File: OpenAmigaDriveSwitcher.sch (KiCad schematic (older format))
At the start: 7 parts, among them J1 PADS, J2 SWITCH, J99 OSHW_LOGO, U1 74LS157, U8 EVEN_CIA_CHIP

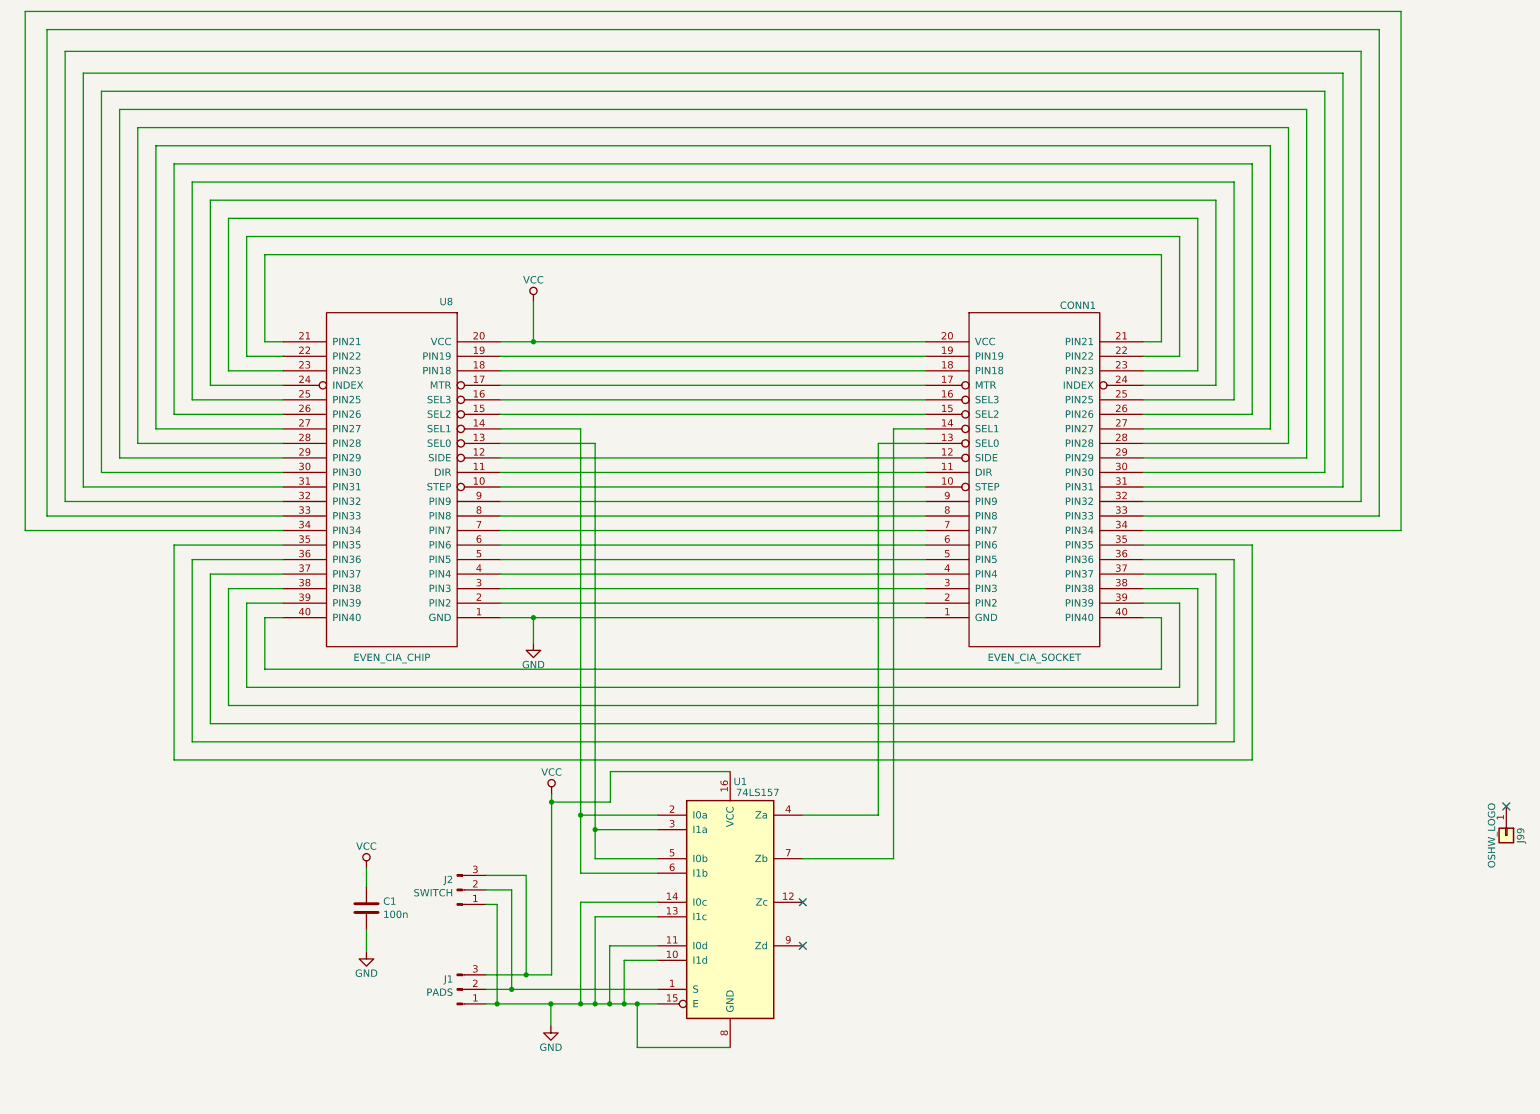
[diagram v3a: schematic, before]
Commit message: Allow swapping DF0 <-> DF2
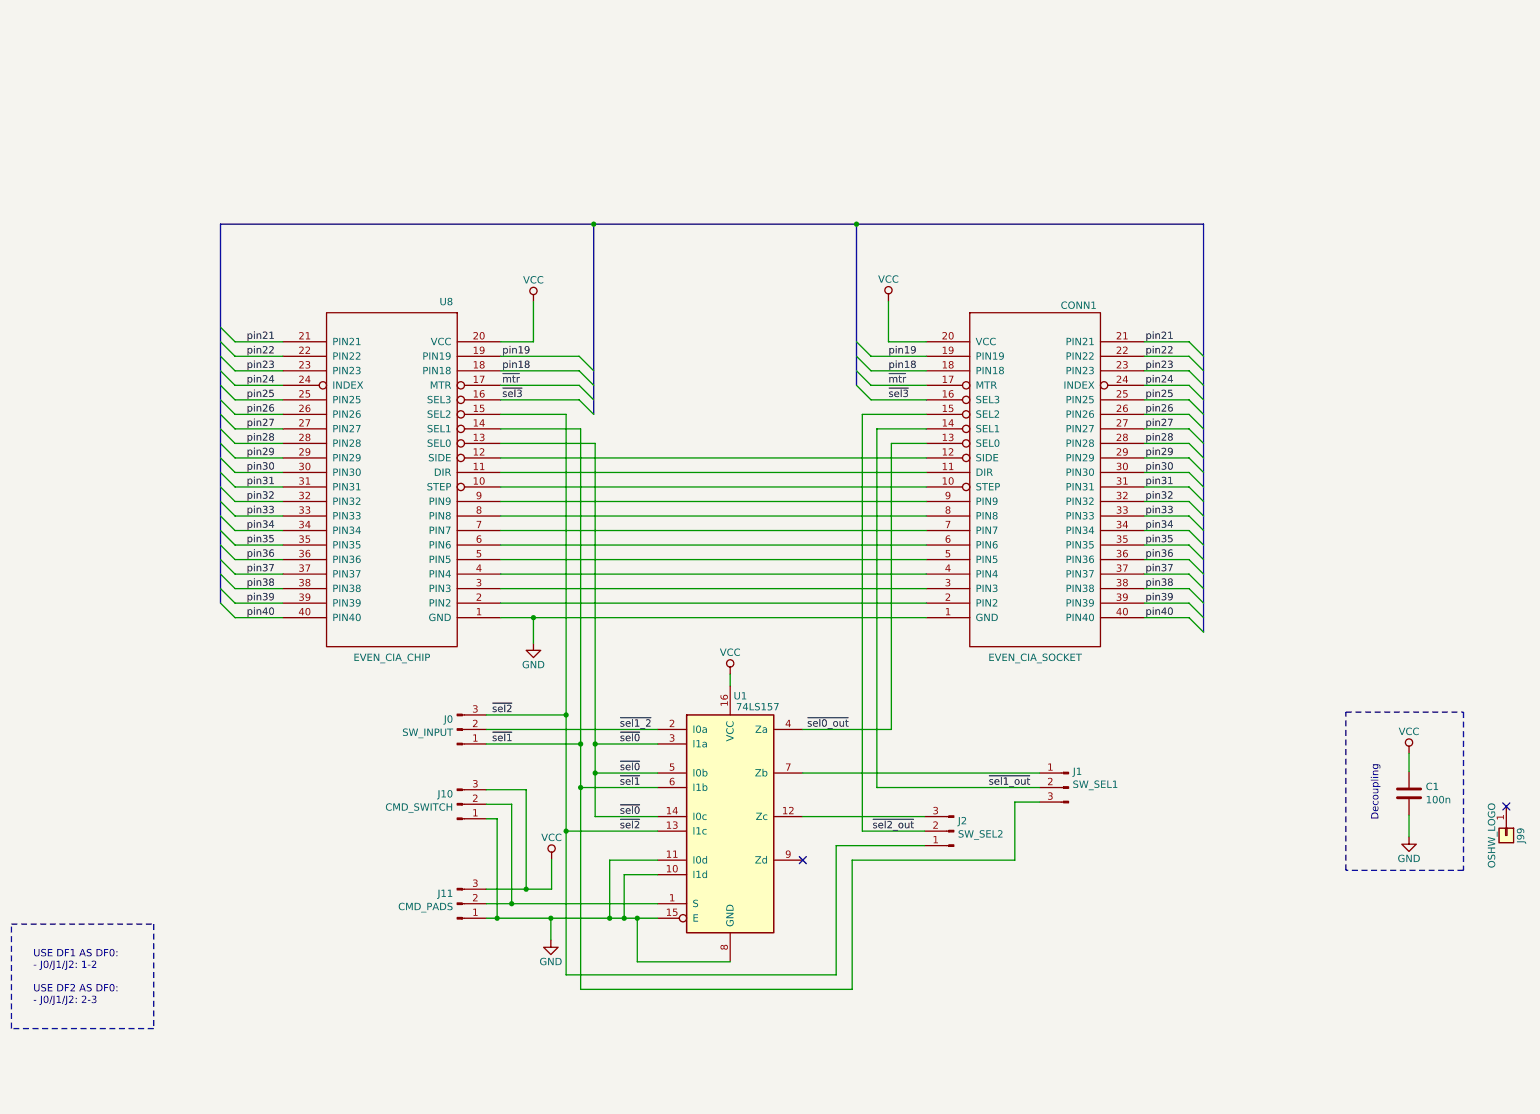
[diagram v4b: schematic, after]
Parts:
- added J0: SW_INPUT, OpenAmigaDriveSwitcher:SolderJumper-3_P1.3mm_Bridged12_RoundedPad1.0x1.5mm, symbol Connector:Conn_01x03_Male
- added J1: SW_SEL1, OpenAmigaDriveSwitcher:SolderJumper-3_P1.3mm_Bridged12_RoundedPad1.0x1.5mm, symbol Connector:Conn_01x03_Male
- added J2: SW_SEL2, OpenAmigaDriveSwitcher:SolderJumper-3_P1.3mm_Bridged12_RoundedPad1.0x1.5mm, symbol Connector:Conn_01x03_Male
- J10: renamed from J2; value SWITCH -> CMD_SWITCH
- J11: renamed from J1; value PADS -> CMD_PADS
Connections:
- net GND: no longer U1.13 (I1c), U1.14 (I0c)
- net ~sel0: now reaches U1.3 (I1a), U1.5 (I0b), U8.13 (SEL0)
- net ~sel0: now also U1.14 (I0c)
- net ~sel1: now reaches U1.6 (I1b), U8.14 (SEL1)
- net ~sel1: now also J0.1 (Pin_1), J1.3 (Pin_3); no longer U1.2 (I0a)
- net ~sel2: now reaches U8.15 (SEL2)
- net ~sel2: now also U1.13 (I1c), J0.3 (Pin_3), J2.1 (Pin_1); no longer CONN1.15 (SEL2)
- net ~sel3: now reaches CONN1.16 (SEL3), U8.16 (SEL3)
- net ~mtr: now reaches CONN1.17 (MTR), U8.17 (MTR)
- net pin18: now reaches CONN1.18 (PIN18), U8.18 (PIN18)
- net pin19: now reaches CONN1.19 (PIN19), U8.19 (PIN19)
- net pin21: now reaches CONN1.21 (PIN21), U8.21 (PIN21)
- net pin22: now reaches CONN1.22 (PIN22), U8.22 (PIN22)
- net pin23: now reaches CONN1.23 (PIN23), U8.23 (PIN23)
- net pin24: now reaches CONN1.24 (INDEX), U8.24 (INDEX)
- net pin25: now reaches CONN1.25 (PIN25), U8.25 (PIN25)
- net pin26: now reaches CONN1.26 (PIN26), U8.26 (PIN26)
- net pin27: now reaches CONN1.27 (PIN27), U8.27 (PIN27)
- net pin28: now reaches CONN1.28 (PIN28), U8.28 (PIN28)
- net pin29: now reaches CONN1.29 (PIN29), U8.29 (PIN29)
- net pin30: now reaches CONN1.30 (PIN30), U8.30 (PIN30)
- net pin31: now reaches CONN1.31 (PIN31), U8.31 (PIN31)
- net pin32: now reaches CONN1.32 (PIN32), U8.32 (PIN32)
- net pin33: now reaches CONN1.33 (PIN33), U8.33 (PIN33)
- net pin34: now reaches CONN1.34 (PIN34), U8.34 (PIN34)
- net pin35: now reaches CONN1.35 (PIN35), U8.35 (PIN35)
- net pin36: now reaches CONN1.36 (PIN36), U8.36 (PIN36)
- net pin37: now reaches CONN1.37 (PIN37), U8.37 (PIN37)
- net pin38: now reaches CONN1.38 (PIN38), U8.38 (PIN38)
- net pin39: now reaches CONN1.39 (PIN39), U8.39 (PIN39)
- net pin40: now reaches CONN1.40 (PIN40), U8.40 (PIN40)
- net ~sel0_out: now reaches CONN1.13 (SEL0), U1.4 (Za)
- net at U1.7 (Zb): now also J1.1 (Pin_1); no longer CONN1.14 (SEL1)
- net at U1.12 (Zc): now also J2.3 (Pin_3)
- new net ~sel1_2: J0.2 (Pin_2), U1.2 (I0a)
- new net ~sel1_out: CONN1.14 (SEL1), J1.2 (Pin_2)
- new net ~sel2_out: CONN1.15 (SEL2), J2.2 (Pin_2)
- no-connect marks 3 -> 2
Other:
- note added: "Decoupling"
- note added: "USE DF1 AS DF0:\n- J0/J1/J2: 1-2\n\nUSE DF2 AS DF0:\n- J0/J1/J2: 2-3\n"
- moved on the sheet: C1, J10, J11, U1

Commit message: Ready for V3
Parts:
- removed J99: OSHW_LOGO, w_logo:Logo_copper_OSHW_6x6mm, symbol OpenAmigaDriveSwitcher-rescue:Conn_01x01
- added P99: OSHW_LOGO, Symbol:OSHW-Logo_5.7x6mm_Copper, symbol conn:CONN_1
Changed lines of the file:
@@
 Sheet 1 1
 Title "OpenAmigaDriveSwitcher"
-Date "2018-09-13"
-Rev "2git"
+Date "2018-12-11"
+Rev "3"
 Comp "SukkoPera"
-Comment1 ""
+Comment1 "Licensed under CERN OHL v.1.2"
 Comment2 ""
 Comment3 ""
@@
 Wire Wire Line
 	10355 5810 10355 5685
-$Comp
-L OpenAmigaDriveSwitcher-rescue:Conn_01x01 J99
-U 1 1 5B317D78
-P 11025 6250
-F 0 "J99" H 11025 6350 50  0000 C CNN
-F 1 "OSHW_LOGO" H 11025 6150 50  0000 C CNN
-F 2 "w_logo:Logo_copper_OSHW_6x6mm" H 11025 6250 50  0001 C CNN
-F 3 "" H 11025 6250 50  0001 C CNN
-	1    11025 6250
-	0    1    1    0
-$EndComp
 NoConn ~ 11025 6050
 Wire Wire Line
@@
 Wire Notes Line
 	730  7580 730  6860
+$Comp
+L conn:CONN_1 P99
+U 1 1 5C101D03
+P 11025 6200
+F 0 "P99" H 10890 6290 40  0000 L CNN
+F 1 "OSHW_LOGO" H 10960 6130 30  0000 C CNN
+F 2 "Symbol:OSHW-Logo_5.7x6mm_Copper" H 11025 6200 50  0001 C CNN
+F 3 "" H 11025 6200 50  0001 C CNN
+	1    11025 6200
+	0    1    1    0
+$EndComp
+Wire Bus Line
+	4740 2040 4740 3350
 Wire Bus Line
 	6550 2040 6550 3150
 Wire Bus Line
-	4740 2040 4740 3350
+	8940 2040 8940 4850
 Wire Bus Line
 	2170 2040 2170 4650
-Wire Bus Line
-	8940 2040 8940 4850
 $EndSCHEMATC
